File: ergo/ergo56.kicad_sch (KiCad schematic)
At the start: 128 parts, among them J1 BAT, J2 AudioJack3_Ground, J3 AudioJack3_Ground, U1 PCA9555PW, U2 Seeeduino Xiao nRF52840

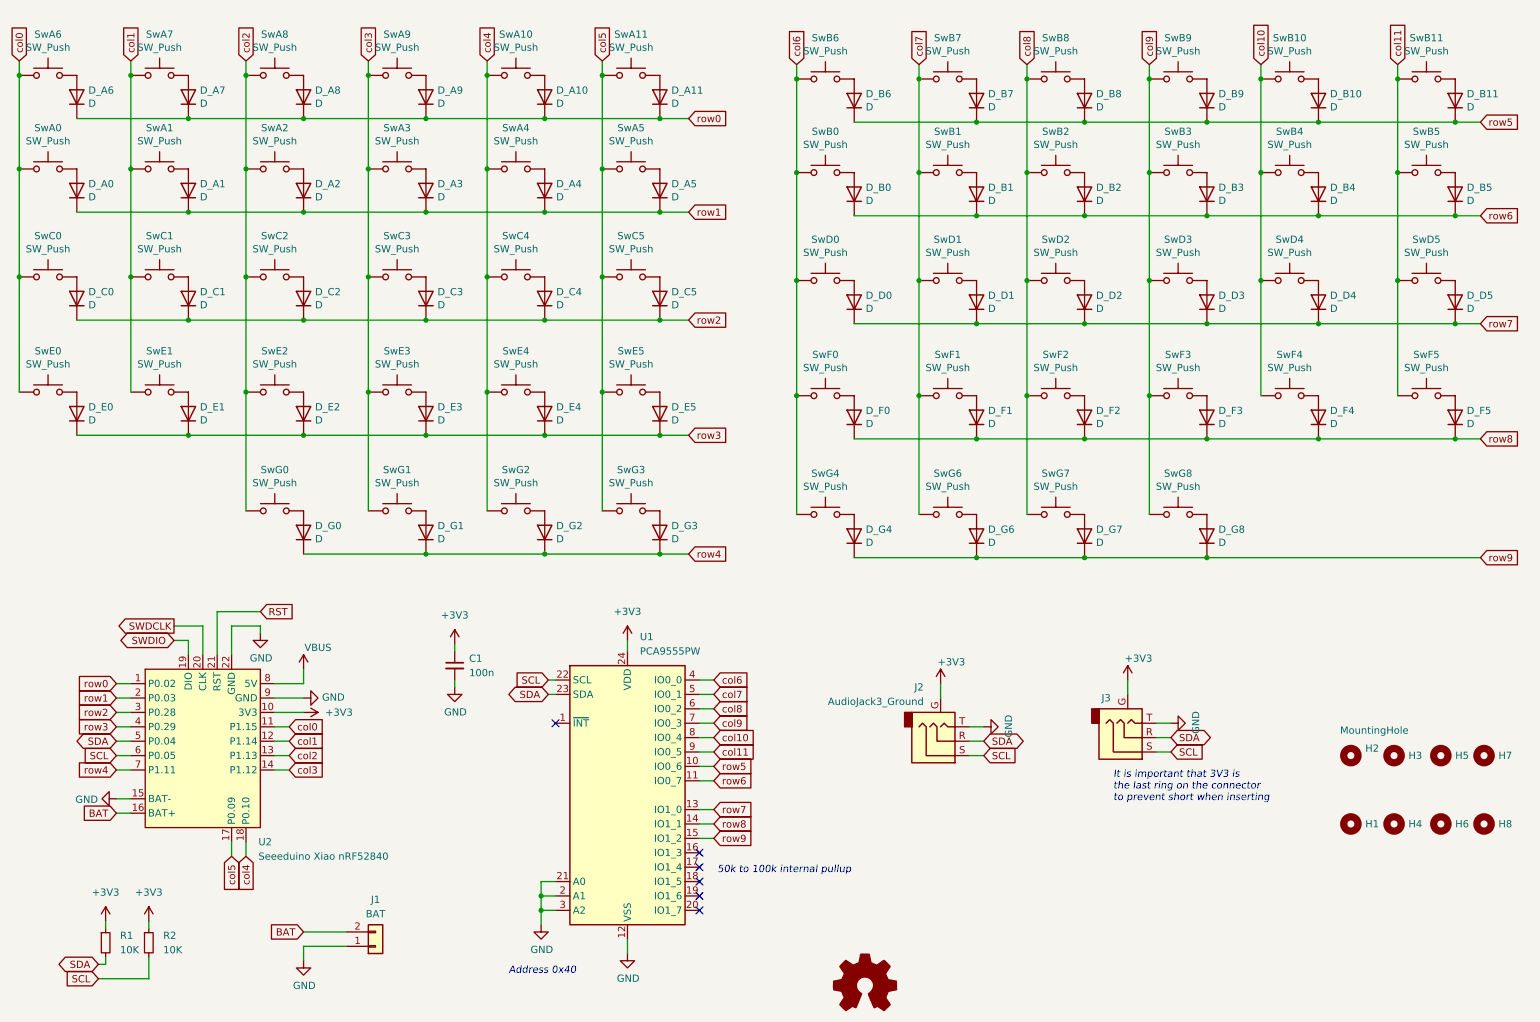
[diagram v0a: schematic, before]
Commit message: schematic done, ERC pass
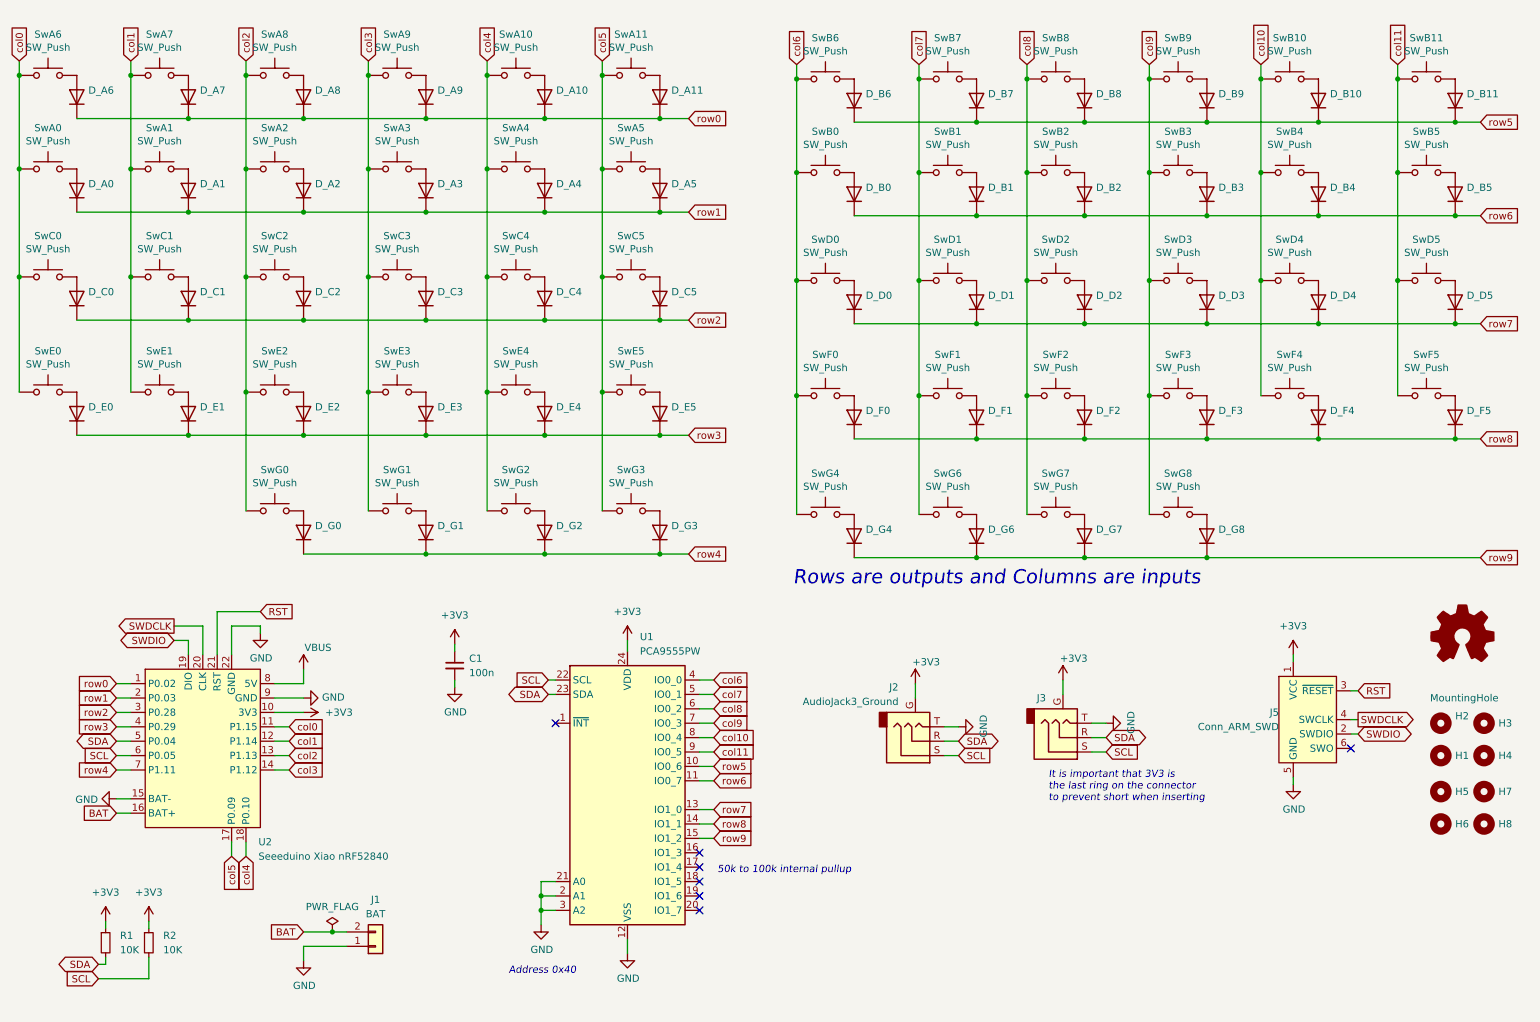
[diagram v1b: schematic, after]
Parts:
- added J5: Conn_ARM_SWD, Connector_PinHeader_1.27mm:PinHeader_2x05_P1.27mm_Vertical_SMD, symbol Connector:Conn_ARM_SWD_TagConnect_TC2030
- D_A0, D_A1, D_A10, D_A11, D_A2, D_A3, D_A4, D_A5, D_A6, D_A7, D_A8, D_A9, D_B0, D_B1, D_B10, D_B11, D_B2, D_B3, D_B4, D_B5, D_B6, D_B7, D_B8, D_B9, D_C0, D_C1, D_C2, D_C3, D_C4, D_C5, D_D0, D_D1, D_D2, D_D3, D_D4, D_D5, D_E0, D_E1, D_E2, D_E3, D_E4, D_E5, D_F0, D_F1, D_F2, D_F3, D_F4, D_F5, D_G0, D_G1, D_G2, D_G3, D_G4, D_G6, D_G7, D_G8: value D -> ~
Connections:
- net +3V3: now also J5.1 (VCC)
- net GND: now also J5.5 (GND)
- net RST: now also J5.3 (~{RESET})
- net SWDCLK: now also J5.4 (SWCLK)
- net SWDIO: now also J5.2 (SWDIO)
- net col0: now also SwA6.1
- net row0: now also D_A10.1 (K), D_A11.1 (K), D_A6.1 (K), D_A7.1 (K), D_A8.1 (K), D_A9.1 (K)
- net row2: now also D_C0.1 (K), D_C1.1 (K), D_C2.1 (K), D_C3.1 (K), D_C4.1 (K), D_C5.1 (K)
- net row3: now also D_E0.1 (K), D_E1.1 (K), D_E2.1 (K), D_E3.1 (K), D_E4.1 (K), D_E5.1 (K)
- net row4: now also D_G0.1 (K), D_G1.1 (K), D_G2.1 (K), D_G3.1 (K)
- no-connect marks 6 -> 7
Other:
- note added: "Rows are outputs and Columns are inputs"
- moved on the sheet: H1, H2, H3, H4, H5, H7, J2, J3

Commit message: all today
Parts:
- H1, H2, H3, H4, H5, H6, H7, H8: footprint (none) -> MountingHole:MountingHole_3.5mm
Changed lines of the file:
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@@
       (effects (font (size 1.27 1.27)) (justify left))
     )
-    (property "Footprint" "" (at 267.97 141.605 0)
+    (property "Footprint" "MountingHole:MountingHole_3.5mm" (at 267.97 141.605 0)
       (effects (font (size 1.27 1.27)) hide)
     )
@@
       (effects (font (size 1.27 1.27)) (justify left) hide)
     )
-    (property "Footprint" "" (at 267.97 159.385 0)
+    (property "Footprint" "MountingHole:MountingHole_3.5mm" (at 267.97 159.385 0)
       (effects (font (size 1.27 1.27)) hide)
     )
@@
       (effects (font (size 1.27 1.27)) (justify left) hide)
     )
-    (property "Footprint" "" (at 275.59 147.32 0)
+    (property "Footprint" "MountingHole:MountingHole_3.5mm" (at 275.59 147.32 0)
       (effects (font (size 1.27 1.27)) hide)
     )
@@
       (effects (font (size 1.27 1.27)) (justify left) hide)
     )
-    (property "Footprint" "" (at 275.59 153.67 0)
+    (property "Footprint" "MountingHole:MountingHole_3.5mm" (at 275.59 153.67 0)
       (effects (font (size 1.27 1.27)) hide)
     )
@@
       (effects (font (size 1.27 1.27)) (justify left) hide)
     )
-    (property "Footprint" "" (at 267.97 153.67 0)
+    (property "Footprint" "MountingHole:MountingHole_3.5mm" (at 267.97 153.67 0)
       (effects (font (size 1.27 1.27)) hide)
     )
@@
       (effects (font (size 1.27 1.27)) (justify left) hide)
     )
-    (property "Footprint" "" (at 275.59 141.605 0)
+    (property "Footprint" "MountingHole:MountingHole_3.5mm" (at 275.59 141.605 0)
       (effects (font (size 1.27 1.27)) hide)
     )
@@
       (effects (font (size 1.27 1.27)) (justify left) hide)
     )
-    (property "Footprint" "" (at 275.59 159.385 0)
+    (property "Footprint" "MountingHole:MountingHole_3.5mm" (at 275.59 159.385 0)
       (effects (font (size 1.27 1.27)) hide)
     )
@@
       (effects (font (size 1.27 1.27)) (justify left) hide)
     )
-    (property "Footprint" "" (at 267.97 147.32 0)
-      (effects (font (size 1.27 1.27)) hide)
-    )
+    (property "Footprint" "MountingHole:MountingHole_3.5mm" (at 267.97 147.32 0)
+      (effects (font (size 1.27 1.27)) hide)
+    )

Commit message: stage
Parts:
- U2: footprint PCM_marbastlib-xp-promicroish:Xiao_nRF52840_ACH -> PCM_marbastlib-xp-promicroish:Xiao_nRF52840_AC_Reflow
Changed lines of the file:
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@@
       (effects (font (size 1.27 1.27)) (justify left))
     )
-    (property "Footprint" "PCM_marbastlib-xp-promicroish:Xiao_nRF52840_ACH" (at 49.53 179.07 0)
+    (property "Footprint" "PCM_marbastlib-xp-promicroish:Xiao_nRF52840_AC_Reflow" (at 49.53 179.07 0)
       (effects (font (size 1.27 1.27)) hide)
     )

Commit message: finish pcb
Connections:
- net col10: now also U1.7 (IO0_3); no longer U1.8 (IO0_4)
- net col11: now also U1.6 (IO0_2); no longer U1.9 (IO0_5)
- net col6: now also U1.11 (IO0_7); no longer U1.4 (IO0_0)
- net col7: now also U1.10 (IO0_6); no longer U1.5 (IO0_1)
- net col8: now also U1.9 (IO0_5); no longer U1.6 (IO0_2)
- net col9: now also U1.8 (IO0_4); no longer U1.7 (IO0_3)
- net row5: now also U1.15 (IO1_2); no longer U1.10 (IO0_6)
- net row6: now also U1.14 (IO1_1); no longer U1.11 (IO0_7)
- net row7: now also U1.4 (IO0_0); no longer U1.13 (IO1_0)
- net row8: now also U1.5 (IO0_1); no longer U1.14 (IO1_1)
- net row9: now also U1.13 (IO1_0); no longer U1.15 (IO1_2)
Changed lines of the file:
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@@
     (effects (font (size 2.5 2.5) italic) (justify left bottom))
   )
-  (global_label "col6" (shape input) (at 139.7 133.985 0) (fields_autoplaced)
-    (effects (font (size 1.27 1.27)) (justify left))
-    (property "Intersheetrefs" "${INTERSHEET_REFS}" (at 146.1433 133.985 0)
+  (global_label "col6" (shape input) (at 139.7 151.765 0) (fields_autoplaced)
+    (effects (font (size 1.27 1.27)) (justify left))
+    (property "Intersheetrefs" "${INTERSHEET_REFS}" (at 146.1433 151.765 0)
       (effects (font (size 1.27 1.27)) (justify left) hide)
     )
@@
     )
   )
-  (global_label "col8" (shape input) (at 139.7 139.065 0) (fields_autoplaced)
-    (effects (font (size 1.27 1.27)) (justify left))
-    (property "Intersheetrefs" "${INTERSHEET_REFS}" (at 146.1433 139.065 0)
+  (global_label "col8" (shape input) (at 139.7 146.685 0) (fields_autoplaced)
+    (effects (font (size 1.27 1.27)) (justify left))
+    (property "Intersheetrefs" "${INTERSHEET_REFS}" (at 146.1433 146.685 0)
       (effects (font (size 1.27 1.27)) (justify left) hide)
     )
@@
     )
   )
-  (global_label "col11" (shape input) (at 139.7 146.685 0) (fields_autoplaced)
-    (effects (font (size 1.27 1.27)) (justify left))
-    (property "Intersheetrefs" "${INTERSHEET_REFS}" (at 147.3528 146.685 0)
-      (effects (font (size 1.27 1.27)) (justify left) hide)
-    )
-  )
-  (global_label "row5" (shape input) (at 139.7 149.225 0) (fields_autoplaced)
-    (effects (font (size 1.27 1.27)) (justify left))
-    (property "Intersheetrefs" "${INTERSHEET_REFS}" (at 146.5062 149.225 0)
+  (global_label "col11" (shape input) (at 139.7 139.065 0) (fields_autoplaced)
+    (effects (font (size 1.27 1.27)) (justify left))
+    (property "Intersheetrefs" "${INTERSHEET_REFS}" (at 147.3528 139.065 0)
+      (effects (font (size 1.27 1.27)) (justify left) hide)
+    )
+  )
+  (global_label "row5" (shape input) (at 139.7 161.925 0) (fields_autoplaced)
+    (effects (font (size 1.27 1.27)) (justify left))
+    (property "Intersheetrefs" "${INTERSHEET_REFS}" (at 146.5062 161.925 0)
       (effects (font (size 1.27 1.27)) (justify left) hide)
     )
@@
     )
   )
-  (global_label "row7" (shape input) (at 139.7 156.845 0) (fields_autoplaced)
-    (effects (font (size 1.27 1.27)) (justify left))
-    (property "Intersheetrefs" "${INTERSHEET_REFS}" (at 146.5062 156.845 0)
+  (global_label "row7" (shape input) (at 139.7 133.985 0) (fields_autoplaced)
+    (effects (font (size 1.27 1.27)) (justify left))
+    (property "Intersheetrefs" "${INTERSHEET_REFS}" (at 146.5062 133.985 0)
       (effects (font (size 1.27 1.27)) (justify left) hide)
     )
@@
     )
   )
-  (global_label "row9" (shape input) (at 139.7 161.925 0) (fields_autoplaced)
-    (effects (font (size 1.27 1.27)) (justify left))
-    (property "Intersheetrefs" "${INTERSHEET_REFS}" (at 146.5062 161.925 0)
+  (global_label "row9" (shape input) (at 139.7 156.845 0) (fields_autoplaced)
+    (effects (font (size 1.27 1.27)) (justify left))
+    (property "Intersheetrefs" "${INTERSHEET_REFS}" (at 146.5062 156.845 0)
       (effects (font (size 1.27 1.27)) (justify left) hide)
     )
@@
     )
   )
-  (global_label "col9" (shape input) (at 139.7 141.605 0) (fields_autoplaced)
-    (effects (font (size 1.27 1.27)) (justify left))
-    (property "Intersheetrefs" "${INTERSHEET_REFS}" (at 146.1433 141.605 0)
+  (global_label "col9" (shape input) (at 139.7 144.145 0) (fields_autoplaced)
+    (effects (font (size 1.27 1.27)) (justify left))
+    (property "Intersheetrefs" "${INTERSHEET_REFS}" (at 146.1433 144.145 0)
       (effects (font (size 1.27 1.27)) (justify left) hide)
     )
@@
     )
   )
-  (global_label "col10" (shape input) (at 139.7 144.145 0) (fields_autoplaced)
-    (effects (font (size 1.27 1.27)) (justify left))
-    (property "Intersheetrefs" "${INTERSHEET_REFS}" (at 147.3528 144.145 0)
+  (global_label "col10" (shape input) (at 139.7 141.605 0) (fields_autoplaced)
+    (effects (font (size 1.27 1.27)) (justify left))
+    (property "Intersheetrefs" "${INTERSHEET_REFS}" (at 147.3528 141.605 0)
       (effects (font (size 1.27 1.27)) (justify left) hide)
     )
@@
     )
   )
-  (global_label "row6" (shape input) (at 139.7 151.765 0) (fields_autoplaced)
-    (effects (font (size 1.27 1.27)) (justify left))
-    (property "Intersheetrefs" "${INTERSHEET_REFS}" (at 146.5062 151.765 0)
-      (effects (font (size 1.27 1.27)) (justify left) hide)
-    )
-  )
-  (global_label "col7" (shape input) (at 139.7 136.525 0) (fields_autoplaced)
-    (effects (font (size 1.27 1.27)) (justify left))
-    (property "Intersheetrefs" "${INTERSHEET_REFS}" (at 146.1433 136.525 0)
+  (global_label "row6" (shape input) (at 139.7 159.385 0) (fields_autoplaced)
+    (effects (font (size 1.27 1.27)) (justify left))
+    (property "Intersheetrefs" "${INTERSHEET_REFS}" (at 146.5062 159.385 0)
+      (effects (font (size 1.27 1.27)) (justify left) hide)
+    )
+  )
+  (global_label "col7" (shape input) (at 139.7 149.225 0) (fields_autoplaced)
+    (effects (font (size 1.27 1.27)) (justify left))
+    (property "Intersheetrefs" "${INTERSHEET_REFS}" (at 146.1433 149.225 0)
       (effects (font (size 1.27 1.27)) (justify left) hide)
     )
@@
     )
   )
-  (global_label "row8" (shape input) (at 139.7 159.385 0) (fields_autoplaced)
-    (effects (font (size 1.27 1.27)) (justify left))
-    (property "Intersheetrefs" "${INTERSHEET_REFS}" (at 146.5062 159.385 0)
-      (effects (font (size 1.27 1.27)) (justify left) hide)
-    )
+  (global_label "row8" (shape input) (at 139.7 136.525 0) (fields_autoplaced)
+    (effects (font (size 1.27 1.27)) (justify left))
+    (property "Intersheetrefs" "${INTERSHEET_REFS}" (at 146.5062 136.525 0)
+      (effects (font (size 1.27 1.27)) (justify left) hide)
+    )
